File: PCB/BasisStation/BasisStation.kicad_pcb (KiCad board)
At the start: 2 copper layers, 150 x 113.5 mm, 21 parts, among them SW4 RESET_BUTTON, U2 ESP32-S3-WROOM-2, X2 JTAG

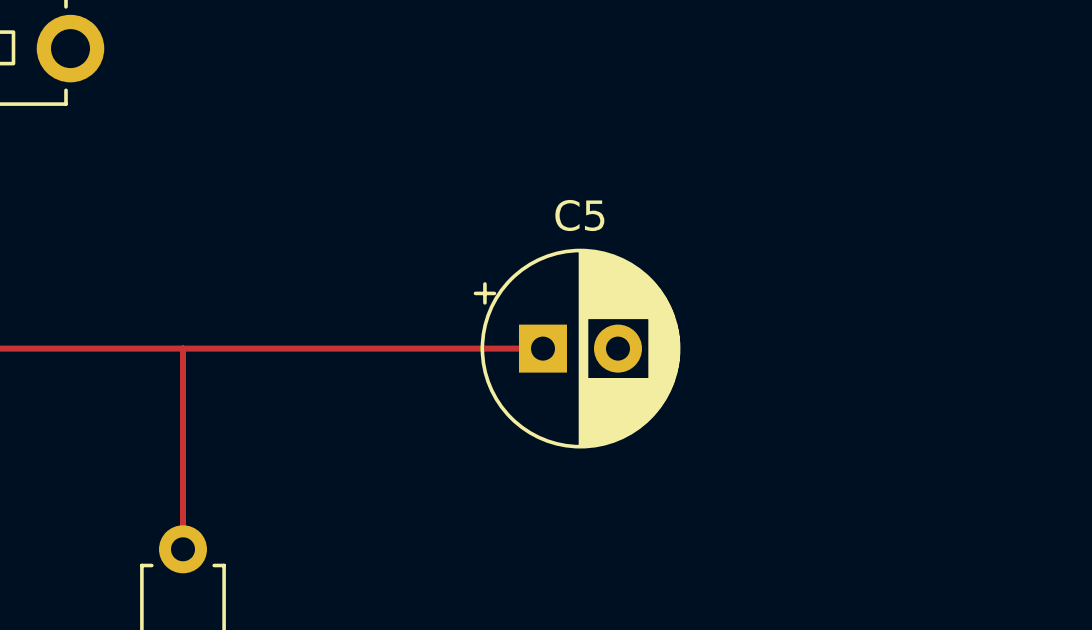
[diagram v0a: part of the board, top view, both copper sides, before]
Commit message: Leiterbahnen editiert
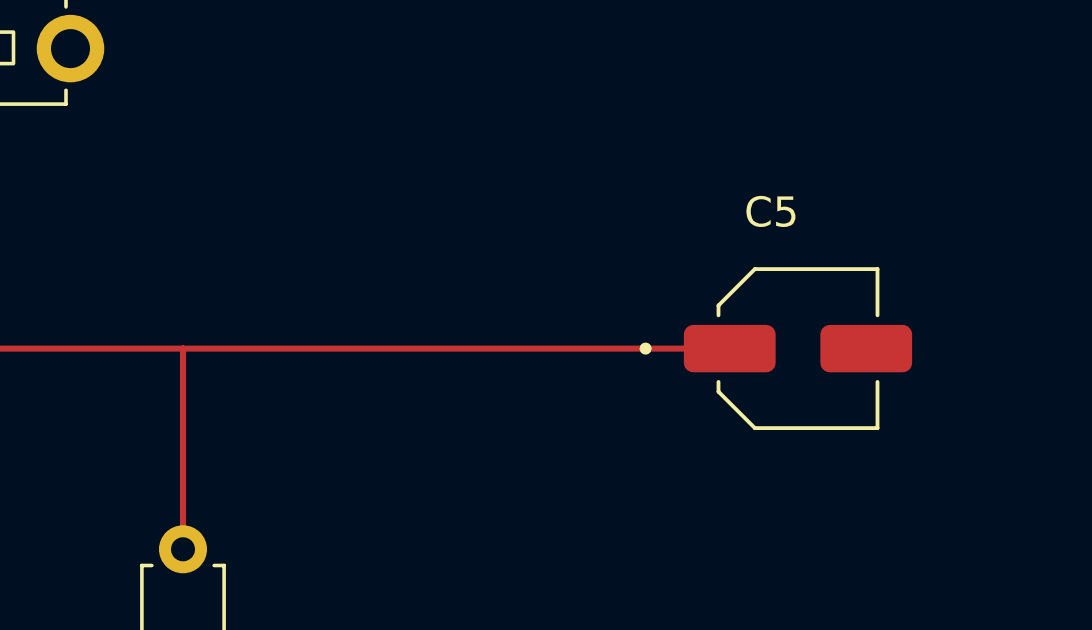
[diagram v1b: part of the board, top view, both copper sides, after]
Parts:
- C5: value 10µF -> 0.47µF; footprint Capacitor_THT:CP_Radial_D6.3mm_P2.50mm -> CUSTOM_Footprint:CAPAE530X565N
- moved C5 8.50 mm to (125.0, 45.5)
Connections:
- C1 pad 1: Net-(PS1-+VOUT) -> +3.3V
- C3 pad 1: Net-(PS1-+VOUT) -> +3.3V
- C7 pad 1: Net-(PS1-+VOUT) -> +3.3V
- R1 pad 2: Net-(D5-A) -> +3.3V
- R5 pad 1: Net-(PS1-+VOUT) -> +3.3V
- R5 pad 2: Net-(SW4-A) -> +3.3V
- SW4 pad 1: GND -> +3.3V
- U2 pad 2: Net-(PS1-+VOUT) -> +3.3V
- U2 pad 3: Net-(SW4-A) -> /EN
- U2 pad 32: Net-(U2-MTCK/GPIO39/CLK_OUT3/SUBSPICS1) -> MTCK
- U2 pad 33: Net-(U2-MTDO/GPIO40/CLK_OUT2) -> MTDO
- U2 pad 34: Net-(U2-MTDI/GPIO41/CLK_OUT1) -> MTDI
- X2 pad 2: MTMS -> Net-(U2-MTMS/GPIO42)
- X3 pad 2: Net-(PS1-+VOUT) -> +3.3V
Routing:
- net Net-(U2-MTMS/GPIO42): track 0.00 -> 114.3 mm
- net MTMS: track 114.3 -> 0.00 mm
- net +3.3V: track 456.5 -> 467.8 mm
- net Net-(D5-A): track 5.08 -> 0.00 mm
- net Net-(U2-MTDO/GPIO40/CLK_OUT2): vias 2 -> 0
- net Net-(U2-MTDI/GPIO41/CLK_OUT1): vias 2 -> 0
- net Net-(U2-MTCK/GPIO39/CLK_OUT3/SUBSPICS1): vias 2 -> 0
- net MTDO: vias 0 -> 2
- net MTDI: vias 0 -> 2
- net MTCK: vias 0 -> 2

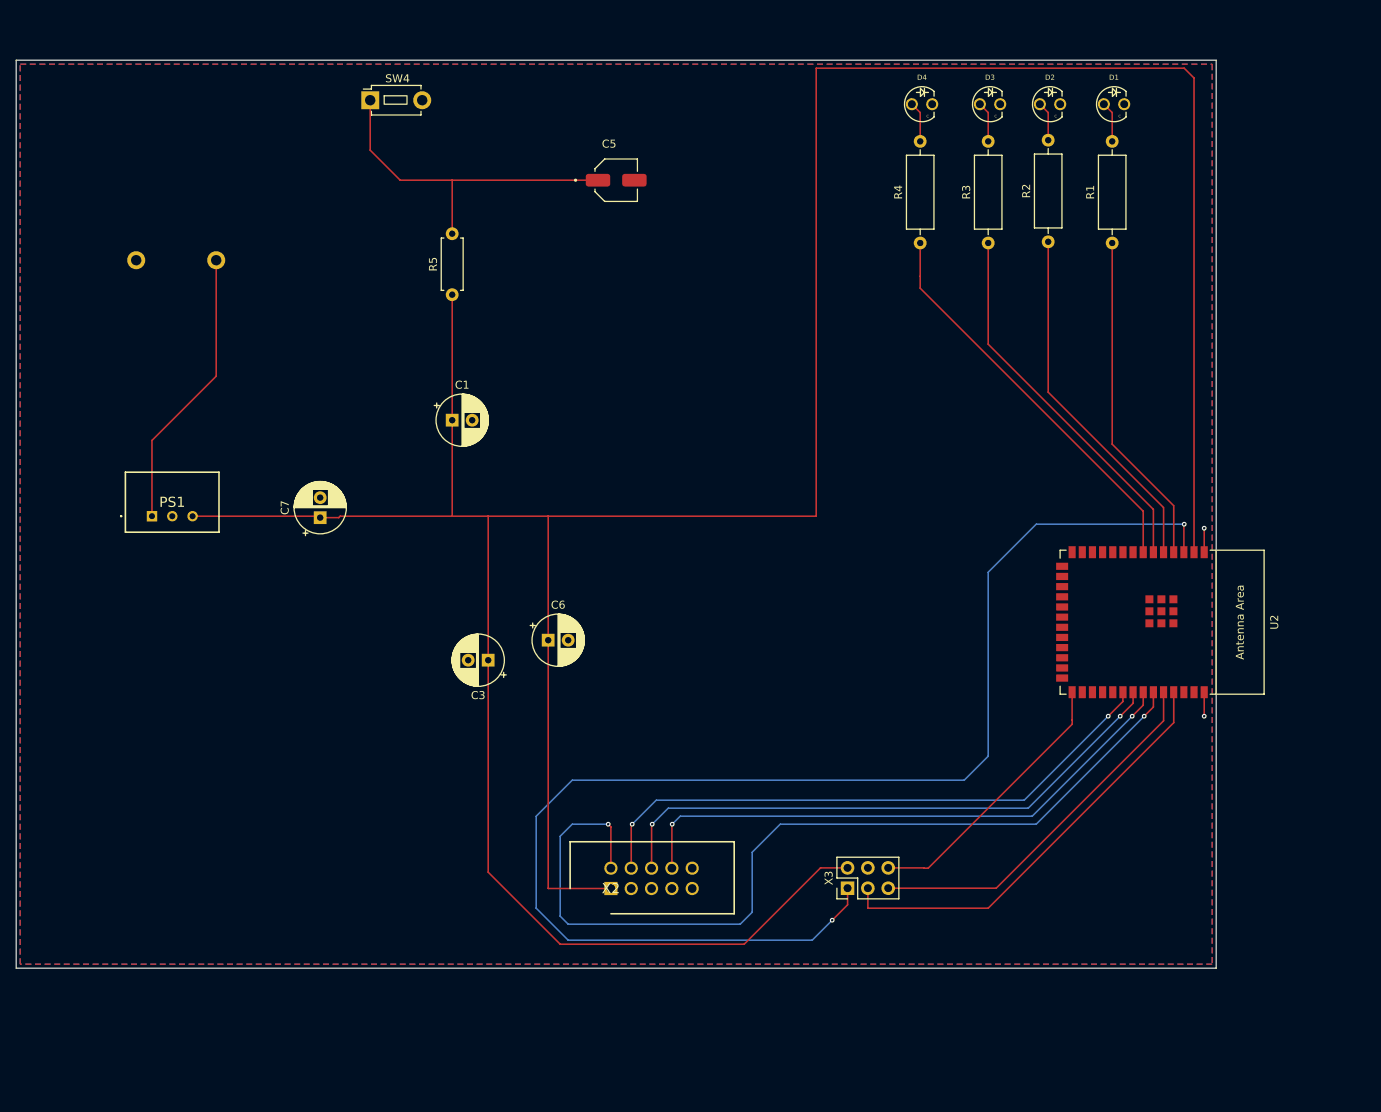
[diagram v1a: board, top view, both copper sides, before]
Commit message: Alte Schaltpläne gelöscht und neue erstellt
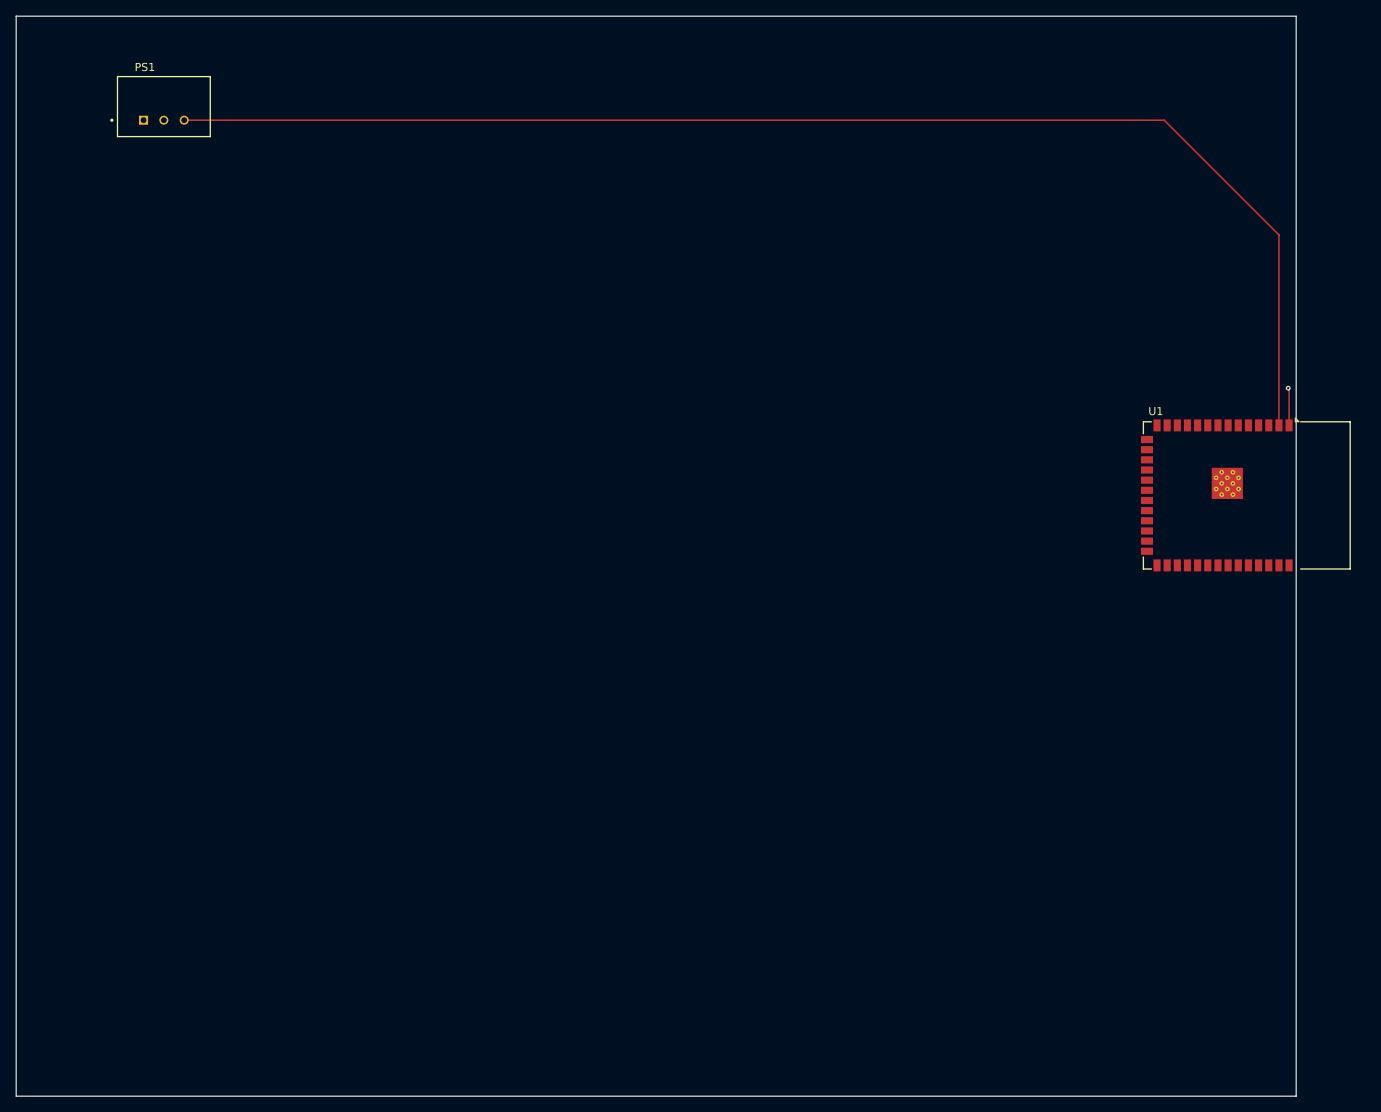
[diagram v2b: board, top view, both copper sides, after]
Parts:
- removed ? (x2): , 
- removed C1: 100µF, Capacitor_THT:CP_Radial_D6.3mm_P2.50mm
- removed C3, C6, C7: 100nF, Capacitor_THT:CP_Radial_D6.3mm_P2.50mm
- removed C5: 0.47µF, CUSTOM_Footprint:CAPAE530X565N
- removed D1, D2, D3, D4: LED, CUSTOM_Footprint:LED-RED-3MM-ROUND
- removed R1, R2, R3, R4: 220, Resistor_THT:R_Axial_DIN0309_L9.0mm_D3.2mm_P12.70mm_Horizontal
- removed R5: 22k, Resistor_THT:R_Axial_DIN0207_L6.3mm_D2.5mm_P7.62mm_Horizontal
- removed SW4: RESET_BUTTON, Button_Switch_THT:SW_PUSH_1P1T_6x3.5mm_H4.3_APEM_MJTP1243
- removed U2: ESP32-S3-WROOM-2, PCM_Espressif:ESP32-S3-WROOM-2
- removed X2: JTAG, CUSTOM_Footprint:WUE_CONNECTOR_SHDR10W64P254_2X5_2036X885X925P
- removed X3: ~, Connector_PinHeader_2.54mm:PinHeader_2x03_P2.54mm_Vertical
- added U1: ESP32-S3-WROOM-1, RF_Module:ESP32-S3-WROOM-1, F.Cu at (203.8, 84.9)
- PS1: footprint TSR1-2433:TSR12433 -> Footprints:CONV_TSR_1-2433E
- moved PS1 51.2 mm to (68.5, 36.3)
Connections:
- PS1 pad 3: +3.3V -> Net-(PS1-+VOUT)
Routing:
- net +3.3V: track 467.8 -> 0.00 mm
- net /EN: track 169.1 -> 0.00 mm, vias 2 -> 0
- net Net-(PS1-+VOUT): track 0.00 -> 166.6 mm
- net Net-(U2-MTMS/GPIO42): track 114.3 -> 0.00 mm, vias 2 -> 0
- net MTCK: track 74.4 -> 0.00 mm, vias 2 -> 0
- net MTDO: track 73.3 -> 0.00 mm, vias 2 -> 0
- net MTDI: track 72.2 -> 0.00 mm, vias 2 -> 0
- net Net-(U2-U0TXD/GPIO43/CLK_OUT1): track 54.1 -> 0.00 mm
- net Net-(U2-GPIO7/TOUCH7/ADC1_CH6): track 50.2 -> 0.00 mm
- net Net-(U2-GPIO6/TOUCH6/ADC1_CH5): track 47.2 -> 0.00 mm
- net Net-(U2-U0RXD/GPIO44/CLK_OUT2): track 46.7 -> 0.00 mm
- net Net-(U2-GPIO5/TOUCH5/ADC1_CH4): track 44.8 -> 0.00 mm
- net Net-(U2-GPIO4/TOUCH4/ADC1_CH3): track 41.8 -> 0.00 mm
- net +12V: track 35.3 -> 0.00 mm
- net Net-(U2-GPIO0/BOOT): track 34.5 -> 0.00 mm
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- removed copper zone on B.Cu, net GND
- removed copper zone on F.Cu, net GND
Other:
- board size 150 x 113.5 mm -> 160 x 135 mm

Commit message: ESP32 Microcontroller geändert
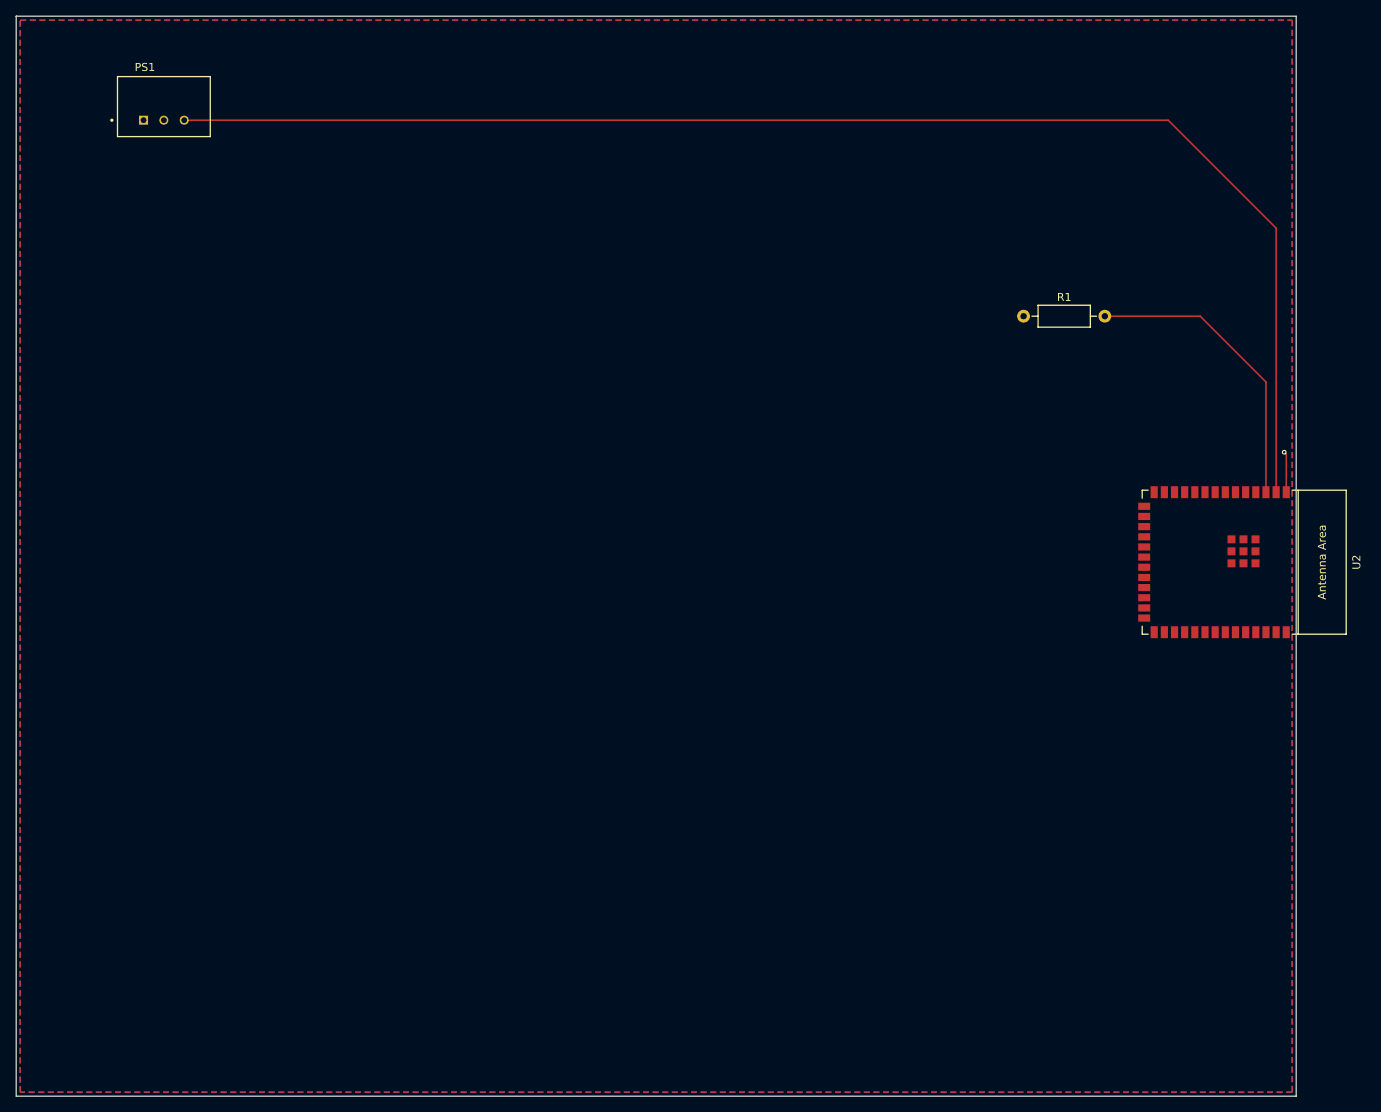
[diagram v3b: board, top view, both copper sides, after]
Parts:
- removed U1: ESP32-S3-WROOM-1, RF_Module:ESP32-S3-WROOM-1
- added R1: 0, Resistor_THT:R_Axial_DIN0207_L6.3mm_D2.5mm_P10.16mm_Horizontal, F.Cu at (175.9, 62.5)
- added U2: ESP32-S3-WROOM-2, PCM_Espressif:ESP32-S3-WROOM-2, F.Cu at (200.5, 93.2)
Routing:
- net Net-(U2-EN): track 0.00 -> 37.3 mm
- net Net-(PS1-+VOUT): track 166.6 -> 175.1 mm
- net GND: track 0.00 -> 5.11 mm, vias 0 -> 1
- net Net-(U1-GND-Pad1): track 4.70 -> 0.00 mm, vias 1 -> 0
- added copper zone on F.Cu, net +12V
- added copper zone on B.Cu, net GND

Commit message: schaltplan überarbeitete
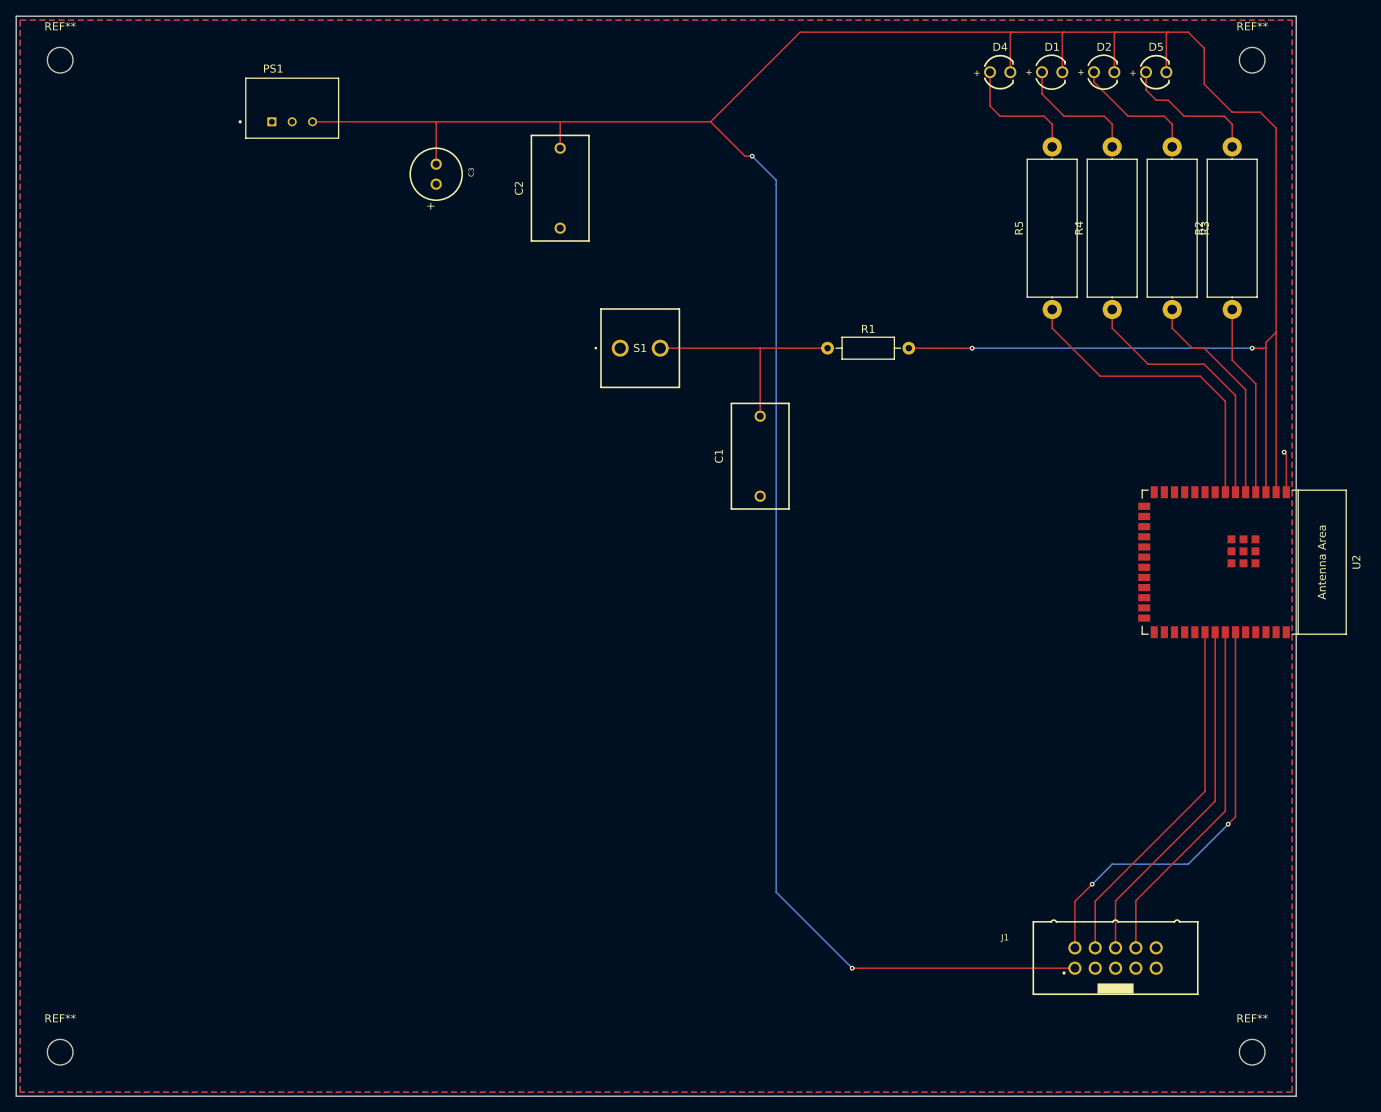
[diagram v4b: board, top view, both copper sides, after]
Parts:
- added C1: WCAP-FTXX_P10, Footprints:WCAP-FTXX_P10L13W7H13, F.Cu at (143.0, 80.0)
- added C2: WCAP-FTXX_P10, Footprints:WCAP-FTXX_P10L13W7H13, F.Cu at (118.0, 46.5)
- added C3: WCAP-PT5H_6.3X5.2, Footprints:WCAP-PT5H_6.3X5.2_DXL_, F.Cu at (102.5, 44.8)
- added D1: RED, Footprints:WL-TMRW_3MM, F.Cu at (179.5, 32.0)
- added D2: BLUE, Footprints:WL-TMRW_3MM, F.Cu at (186.0, 32.0)
- added D4: GREEN, Footprints:WL-TMRC_3MM, F.Cu at (173.0, 32.0)
- added D5: YELLOW, Footprints:WL-TMRC_3MM, F.Cu at (192.5, 32.0)
- added J1: Conn_02x05_Odd_Even, Footprints:61201021621, F.Cu at (187.4, 142.7)
- added R2: 220, Resistor_THT:R_Axial_DIN0617_L17.0mm_D6.0mm_P20.32mm_Horizontal, F.Cu at (202.0, 61.7)
- added R3: 220, Resistor_THT:R_Axial_DIN0617_L17.0mm_D6.0mm_P20.32mm_Horizontal, F.Cu at (194.5, 41.3)
- added R4: 220, Resistor_THT:R_Axial_DIN0617_L17.0mm_D6.0mm_P20.32mm_Horizontal, F.Cu at (187.0, 61.7)
- added R5: 220, Resistor_THT:R_Axial_DIN0617_L17.0mm_D6.0mm_P20.32mm_Horizontal, F.Cu at (179.5, 61.7)
- added REF**: MountingHole_3.2mm_M3, MountingHole:MountingHole_3.2mm_M3, F.Cu at (55.5, 30.5)
- added REF**: MountingHole_3.2mm_M3, MountingHole:MountingHole_3.2mm_M3, F.Cu at (204.5, 30.5)
- added REF**: MountingHole_3.2mm_M3, MountingHole:MountingHole_3.2mm_M3, F.Cu at (204.5, 154.5)
- added REF**: MountingHole_3.2mm_M3, MountingHole:MountingHole_3.2mm_M3, F.Cu at (55.5, 154.5)
- added S1: 1543-650-149, Footprints:1543650149, F.Cu at (125.5, 66.5)
- U2: footprint PCM_Espressif:ESP32-S3-WROOM-2 -> Footprints:ESP32-S3-WROOM-2_NEW
- moved R1 24.8 mm to (151.4, 66.5)
- moved PS1 16.0 mm to (84.5, 36.5)
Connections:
- PS1 pad 3: Net-(PS1-+VOUT) -> +3V3
- R1 pad 1: GND -> Net-(C1-Pad2)
- R1 pad 2: Net-(U2-EN) -> Net-(PS1-+VOUT)
- U2 pad 2: Net-(PS1-+VOUT) -> +3V3
- U2 pad 3: Net-(U2-EN) -> EN
- U2 pad 32: unconnected-(U2-MTCK/GPIO39/CLK_OUT3/SUBSPICS1-Pad32) -> MTCK
- U2 pad 33: unconnected-(U2-MTDO/GPIO40/CLK_OUT2-Pad33) -> MTDO
- U2 pad 34: unconnected-(U2-MTDI/GPIO41/CLK_OUT1-Pad34) -> MTDI
- U2 pad 35: unconnected-(U2-MTMS/GPIO42-Pad35) -> MTMS
- U2 pad 4: unconnected-(U2-GPIO4/TOUCH4/ADC1_CH3-Pad4) -> Net-(U2-GPIO4/TOUCH4/ADC1_CH3)
- U2 pad 5: unconnected-(U2-GPIO5/TOUCH5/ADC1_CH4-Pad5) -> Net-(U2-GPIO5/TOUCH5/ADC1_CH4)
- U2 pad 6: unconnected-(U2-GPIO6/TOUCH6/ADC1_CH5-Pad6) -> Net-(U2-GPIO6/TOUCH6/ADC1_CH5)
- U2 pad 7: unconnected-(U2-GPIO7/TOUCH7/ADC1_CH6-Pad7) -> Net-(U2-GPIO7/TOUCH7/ADC1_CH6)
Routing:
- net +3V3: track 0.00 -> 413.8 mm, vias 0 -> 4
- net Net-(PS1-+VOUT): track 175.1 -> 0.00 mm
- net MTMS: track 0.00 -> 53.3 mm, vias 0 -> 2
- net MTCK: track 0.00 -> 45.1 mm
- net MTDO: track 0.00 -> 44.6 mm
- net MTDI: track 0.00 -> 44.1 mm
- net Net-(U2-GPIO7/TOUCH7/ADC1_CH6): track 0.00 -> 39.1 mm
- net Net-(U2-EN): track 37.3 -> 0.00 mm
- net Net-(U2-GPIO6/TOUCH6/ADC1_CH5): track 0.00 -> 33.3 mm
- net Net-(C1-Pad2): track 0.00 -> 29.4 mm
- net Net-(U2-GPIO5/TOUCH5/ADC1_CH4): track 0.00 -> 27.5 mm
- net Net-(U2-GPIO4/TOUCH4/ADC1_CH3): track 0.00 -> 24.1 mm
- net Net-(D5-Pad1): track 0.00 -> 17.6 mm
- net Net-(D2-A): track 0.00 -> 16.0 mm
- net Net-(D1-A): track 0.00 -> 15.9 mm
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- added copper zone on F.Cu, net GND
- removed copper zone on F.Cu, net +12V
